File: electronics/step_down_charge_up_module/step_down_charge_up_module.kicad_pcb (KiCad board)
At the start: 2 copper layers, 64.1 x 29.8 mm, 55 parts, among them J101 CONN_01X03, J102 CONN_01X03, J103 CONN_01X02, J104 CONN_01X02, J105 CONN_01X02, J106 CONN_01X02, J107 CONN_01X03, J108 CONN_01X03, J109 CONN_01X03, J110 CONN_01X03, Q101 Q_NMOS_GSD, Q102 Q_NMOS_GSD, Q501 2N3906, Q502 AO3401A, Q503 2N3906, Q504 Q_PMOS_GSD, SW101 SW_Push, SW102 SW_Push, U201 MP2315, U301 MCP73831, U401 SX1308, U601 ATTINY84-20SSU

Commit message: Checkpoint
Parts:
- added P101: SYMBOL, Board_Outlines:Board_Outline_65x48mm, F.Cu at (108.5, 46.9)
- moved R503 70.6 mm to (166.9, 60.2), turned to 90 degrees
- moved Q501 68.1 mm to (156.6, 67.1)
- moved Q502 68.1 mm to (160.4, 67.1)
- moved Q503 68.1 mm to (152.8, 67.1)
- moved Q102 64.3 mm to (164.3, 59.6), turned to 270 degrees
- moved R502 42.7 mm to (161.2, 60.8)
- moved R501 42.6 mm to (156.7, 60.8)
- moved J103 36.2 mm to (125.6, 65.9), turned to 270 degrees
- moved J106 35.5 mm to (150.4, 85.0)
- moved C602 35.2 mm to (125.6, 50.0), turned to 90 degrees
- moved Q101 29.2 mm to (140.0, 59.4), turned to 90 degrees
- moved U601 28.6 mm to (126.9, 57.0)
- moved J105 27.9 mm to (144.0, 82.4), turned to 0 degrees
- moved R102 26.3 mm to (137.2, 59.2), turned to 90 degrees
- moved J107 25.4 mm to (119.3, 59.6), turned to 180 degrees
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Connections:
- U601 pad 10: Net-(U601-Pad10) -> (no net)
- U601 pad 6: Net-(U601-Pad6) -> (no net)
- U601 pad 8: Net-(U601-Pad8) -> (no net)
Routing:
- net /step_down/PWR_IN: track 23.7 -> 0.34 mm, vias 1 -> 0
- net /supervisor/BATT: track 0.00 -> 19.5 mm, vias 0 -> 2
- net /supervisor/~ON_WALL: track 0.00 -> 16.9 mm, vias 0 -> 2
- net /supervisor/~ON_BUTTON: track 0.00 -> 16.4 mm, vias 0 -> 1
- net /charge/CHG_PWR: track 24.1 -> 9.23 mm, vias 2 -> 0
- net /supervisor/~OFF_BUTTON: track 0.00 -> 13.9 mm, vias 0 -> 1
- net /supervisor/5V_EN: track 0.00 -> 13.2 mm
- net /supervisor/SHUTDOWN: track 0.00 -> 12.1 mm, vias 0 -> 1
- net Net-(C203-Pad2): track 11.7 -> 0.00 mm
- net /load_switch/OUT: track 0.00 -> 9.40 mm
- net /supervisor/SCL: track 0.00 -> 8.46 mm, vias 0 -> 2
- net /supervisor/~WAKEUP_ON_RETURN: track 0.00 -> 8.29 mm
- net Net-(R202-Pad1): track 7.96 -> 0.00 mm, vias 2 -> 0
- net Net-(C602-Pad1): track 0.00 -> 6.89 mm
- net /supervisor/SDA: track 0.00 -> 5.77 mm
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- added copper zone on F.Cu, net GND
- removed copper zone on F.Cu, net /step_down/PWR_IN
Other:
- board size 64.1 x 29.8 mm -> 65 x 48 mm
- board text added: "Auto-Wakeup"
- board text added: "SCL SDA SHDN"

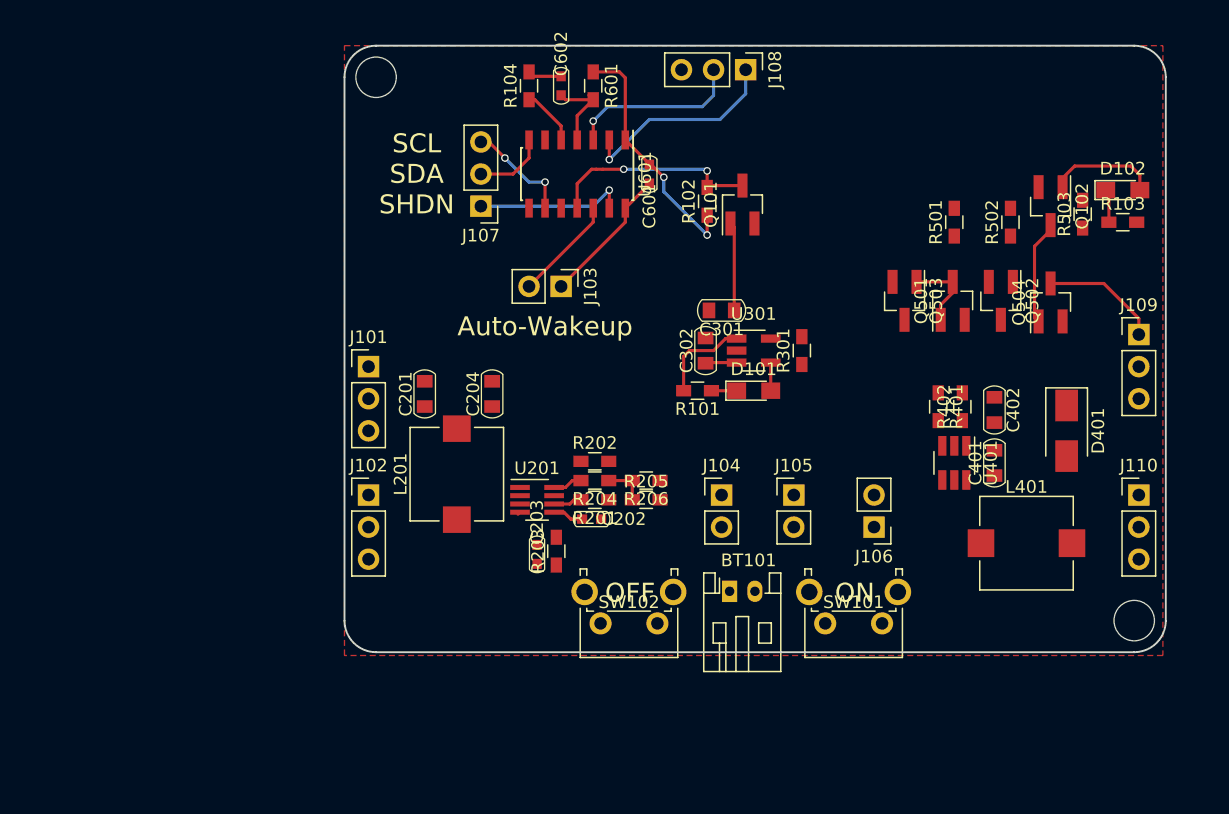
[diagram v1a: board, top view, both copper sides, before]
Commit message: Finish routing, add ICSP port.
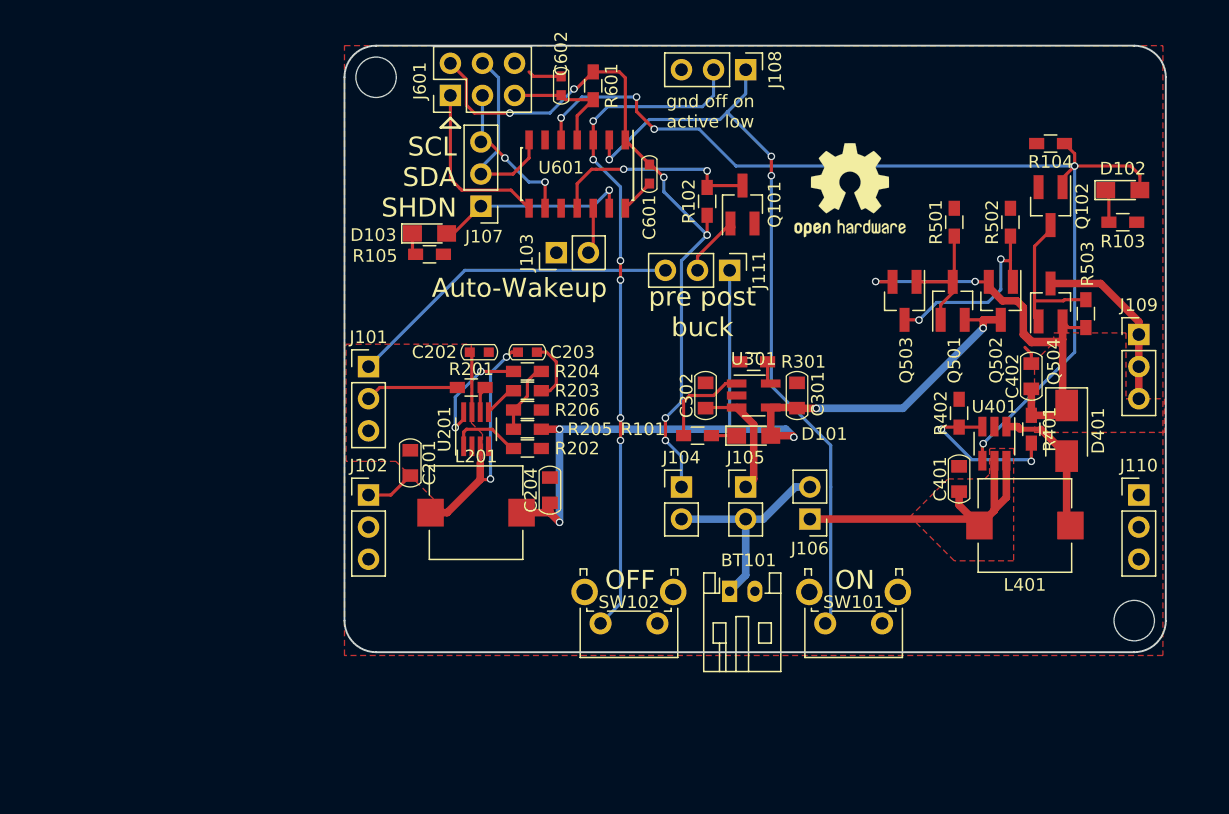
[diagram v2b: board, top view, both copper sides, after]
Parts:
- added D103: LED, LEDs:LED_0805_HandSoldering, F.Cu at (115.2, 61.7)
- added J111: CONN_01X03, Pin_Headers:Pin_Header_Straight_1x03_Pitch2.54mm, F.Cu at (138.9, 64.6)
- added J601: CONN_02X03, Pin_Headers:Pin_Header_Straight_2x03_Pitch2.54mm, F.Cu at (116.8, 50.8)
- added P102: OSHW, Symbols:OSHW-Logo2_9.8x8mm_SilkScreen, F.Cu at (148.5, 58.3)
- added R105: 1k, Resistors_SMD:R_0603_HandSoldering, F.Cu at (115.2, 63.4)
- P101: value SYMBOL -> Outline
- R205: value 402k -> 40.2k
- moved R104 41.5 mm to (164.3, 54.6), turned to 180 degrees
- moved C203 16.0 mm to (122.9, 71.1), turned to 180 degrees
- moved C202 15.9 mm to (119.1, 71.1)
- moved R201 13.2 mm to (118.5, 73.9), turned to 0 degrees
- moved R203 12.9 mm to (122.9, 74.2), turned to 180 degrees
- moved R205 10.9 mm to (122.9, 77.2)
- moved R206 10.9 mm to (122.9, 75.7)
- moved R204 10.2 mm to (122.9, 72.6)
- moved C301 9.00 mm to (144.3, 74.5), turned to 90 degrees
- moved C204 8.89 mm to (124.7, 82.0)
- moved R503 7.88 mm to (167.1, 68.1)
- moved R401 7.58 mm to (162.8, 77.2)
- moved U201 7.38 mm to (118.9, 77.2), turned to 90 degrees
- moved C201 5.58 mm to (113.7, 79.9), turned to 270 degrees
- moved R202 5.43 mm to (122.9, 78.7)
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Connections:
- net Net-(C602-Pad1) renamed /supervisor/RESET
- Q101 pad 1: /charge/CHG_PWR -> Net-(J111-Pad2)
- U601 pad 8: (no net) -> /supervisor/MISO
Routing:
- net /supervisor/5V_EN: track 13.2 -> 83.2 mm, vias 0 -> 5
- net /charge/CHG_PWR: track 9.23 -> 75.3 mm, vias 0 -> 5
- net /supervisor/~ON_BUTTON: track 16.4 -> 60.7 mm, vias 1 -> 3
- net /load_switch/BOOSTED_BATT_IN: track 0.72 -> 43.2 mm, vias 0 -> 2
- net /supervisor/~OFF_BUTTON: track 13.9 -> 53.7 mm, vias 1 -> 6
- net /supervisor/BATT: track 19.5 -> 56.8 mm, vias 2 -> 6
- net /step_down/PWR_IN: track 0.34 -> 34.2 mm
- net /step_up/PWR_IN: track 0.00 -> 26.8 mm
- net Net-(C203-Pad2): track 0.00 -> 25.1 mm, vias 0 -> 2
- net Net-(BT101-Pad1): track 0.00 -> 17.5 mm
- net Net-(Q502-Pad1): track 1.33 -> 16.9 mm, vias 0 -> 2
- net /supervisor/MISO: track 0.00 -> 13.8 mm
- net Net-(R401-Pad2): track 0.00 -> 12.9 mm, vias 0 -> 2
- net Net-(D401-Pad2): track 0.00 -> 11.4 mm
- net /supervisor/SDA: track 5.77 -> 15.7 mm
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- added copper zone on F.Cu, net /load_switch/BOOSTED_BATT_IN
- added copper zone on F.Cu, net /step_down/PWR_IN
- added copper zone on F.Cu, net /step_up/PWR_IN
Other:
- board text added: "gnd off on active low"
- board text added: "pre post buck"

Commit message: Swap LED resistor locations, enlarge handsoldering inductor
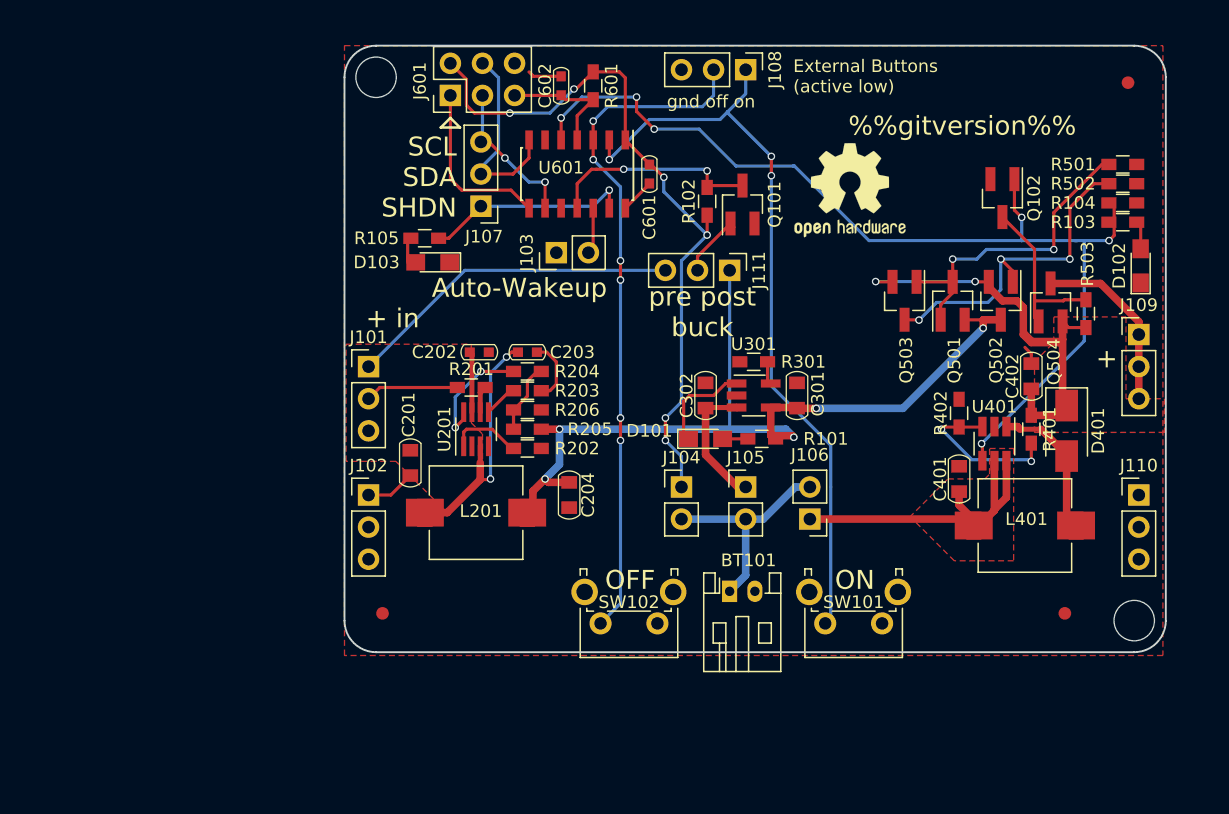
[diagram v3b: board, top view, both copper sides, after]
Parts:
- added P103: Fid, Fiducials:Fiducial_1mm_Dia_2.54mm_Outer_CopperTop, F.Cu at (170.5, 49.8)
- added P104: Fid, Fiducials:Fiducial_1mm_Dia_2.54mm_Outer_CopperTop, F.Cu at (111.5, 91.8)
- added P105: Fid, Fiducials:Fiducial_1mm_Dia_2.54mm_Outer_CopperTop, F.Cu at (165.5, 91.8)
- moved R501 14.1 mm to (170.1, 56.3), turned to 0 degrees
- moved R502 9.40 mm to (170.1, 57.8), turned to 0 degrees
- moved R104 7.40 mm to (170.1, 59.3), turned to 0 degrees
- moved D102 6.16 mm to (171.5, 64.3), turned to 90 degrees
- moved R101 5.09 mm to (141.5, 78.0)
- moved Q102 3.86 mm to (160.5, 58.9)
- moved D101 3.82 mm to (137.0, 78.0)
- moved D103 2.30 mm to (115.4, 64.0), turned to 180 degrees
- moved C204 1.57 mm to (126.2, 82.4), turned to 270 degrees
- moved R105 1.33 mm to (114.8, 62.1), turned to 180 degrees
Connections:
- D101 pad 1: Net-(D101-Pad1) -> /charge/~CHARGING
- D101 pad 2: /charge/CHG_PWR -> Net-(D101-Pad2)
- D102 pad 1: Net-(D102-Pad1) -> GND
- D102 pad 2: /supervisor/5V_EN -> Net-(D102-Pad2)
- D103 pad 1: Net-(D103-Pad1) -> GND
- D103 pad 2: /supervisor/SHUTDOWN -> Net-(D103-Pad2)
- R101 pad 1: Net-(D101-Pad1) -> /charge/CHG_PWR
- R101 pad 2: /charge/~CHARGING -> Net-(D101-Pad2)
- R103 pad 1: Net-(D102-Pad1) -> /supervisor/5V_EN
- R103 pad 2: GND -> Net-(D102-Pad2)
- R105 pad 1: Net-(D103-Pad1) -> /supervisor/SHUTDOWN
- R105 pad 2: GND -> Net-(D103-Pad2)
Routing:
- net Net-(Q501-Pad1): track 9.93 -> 25.4 mm, vias 0 -> 2
- net Net-(Q502-Pad1): track 16.9 -> 28.2 mm, vias 2 -> 3
- net Net-(D102-Pad1): track 2.64 -> 0.00 mm
- net /supervisor/5V_EN: track 83.2 -> 80.8 mm, vias 5 -> 6
- net Net-(D102-Pad2): track 0.00 -> 2.19 mm
- net Net-(R201-Pad2): track 2.17 -> 4.28 mm
- net Net-(D103-Pad2): track 0.00 -> 2.01 mm
- net Net-(D101-Pad1): track 2.00 -> 0.00 mm
- net Net-(D101-Pad2): track 0.00 -> 1.99 mm
- net Net-(D103-Pad1): track 1.75 -> 0.00 mm
- net /load_switch/~EN: track 12.4 -> 13.7 mm
- net /charge/CHG_PWR: track 75.3 -> 74.2 mm
- net /charge/BATT: track 9.60 -> 10.5 mm
- net /supervisor/SHUTDOWN: track 15.7 -> 16.5 mm
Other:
- board text added: "%%gitversion%%"
- board text added: "+"
- board text added: "+ in"
- board text added: "External Buttons (active low)"
- board text added: "github.com/google/makerspace-partsbin step_down_charge_up_module"
- board text added: "gnd off on"
- board text removed: "gnd off on active low"

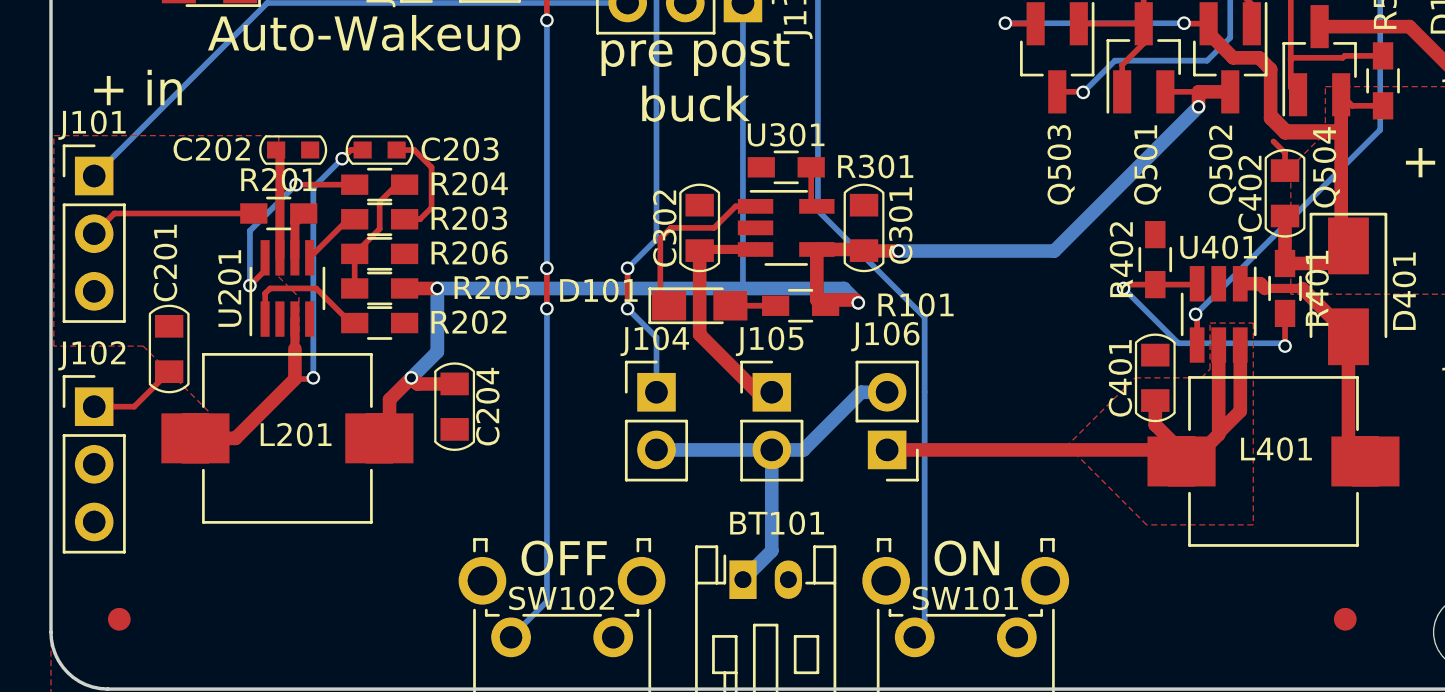
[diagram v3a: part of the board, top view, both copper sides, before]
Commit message: Swap to 1206 caps for easier prototyping.
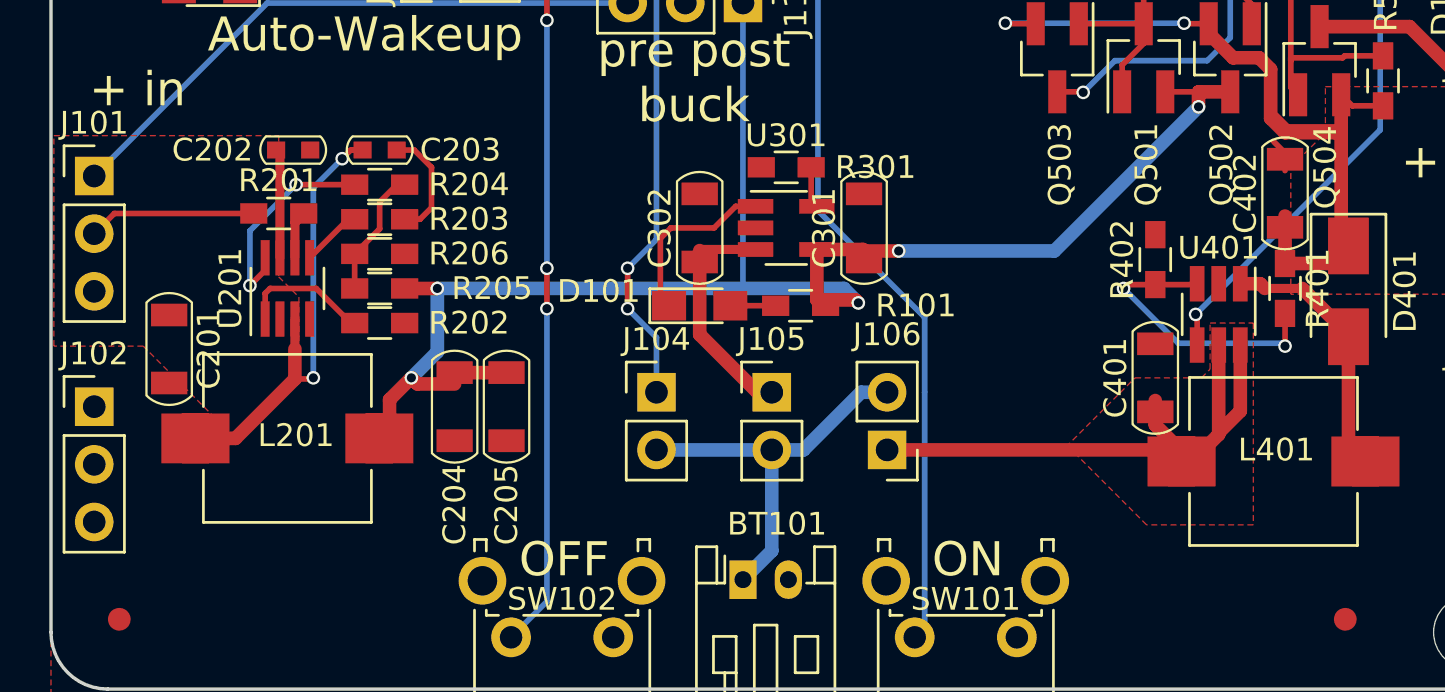
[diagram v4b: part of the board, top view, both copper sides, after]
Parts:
- added C205: 22u, Capacitors_SMD_Round:C_1206, F.Cu at (128.5, 82.4)
- C201, C204, C401, C402: footprint Capacitors_SMD_Round:C_0805 -> Capacitors_SMD_Round:C_1206
- C301, C302: value C -> 4.7u; footprint Capacitors_SMD_Round:C_0805 -> Capacitors_SMD_Round:C_1206
- R301: value R -> 2k
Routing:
- net GND: track 10.9 -> 6.92 mm
- net /charge/CHG_PWR: track 74.2 -> 76.5 mm
